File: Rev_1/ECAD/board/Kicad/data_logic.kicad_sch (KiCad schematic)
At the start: 69 parts, among them SW300 SW_Push, SW301 SW_Push, SW302 SW_Push, SW303 SW_Push, U300 AT28C64B-15PU, U301 74HC245, U302 74HC595, U303 74HC245, U304 4076B, U305 4076B, U306 4076B, U307 4076B

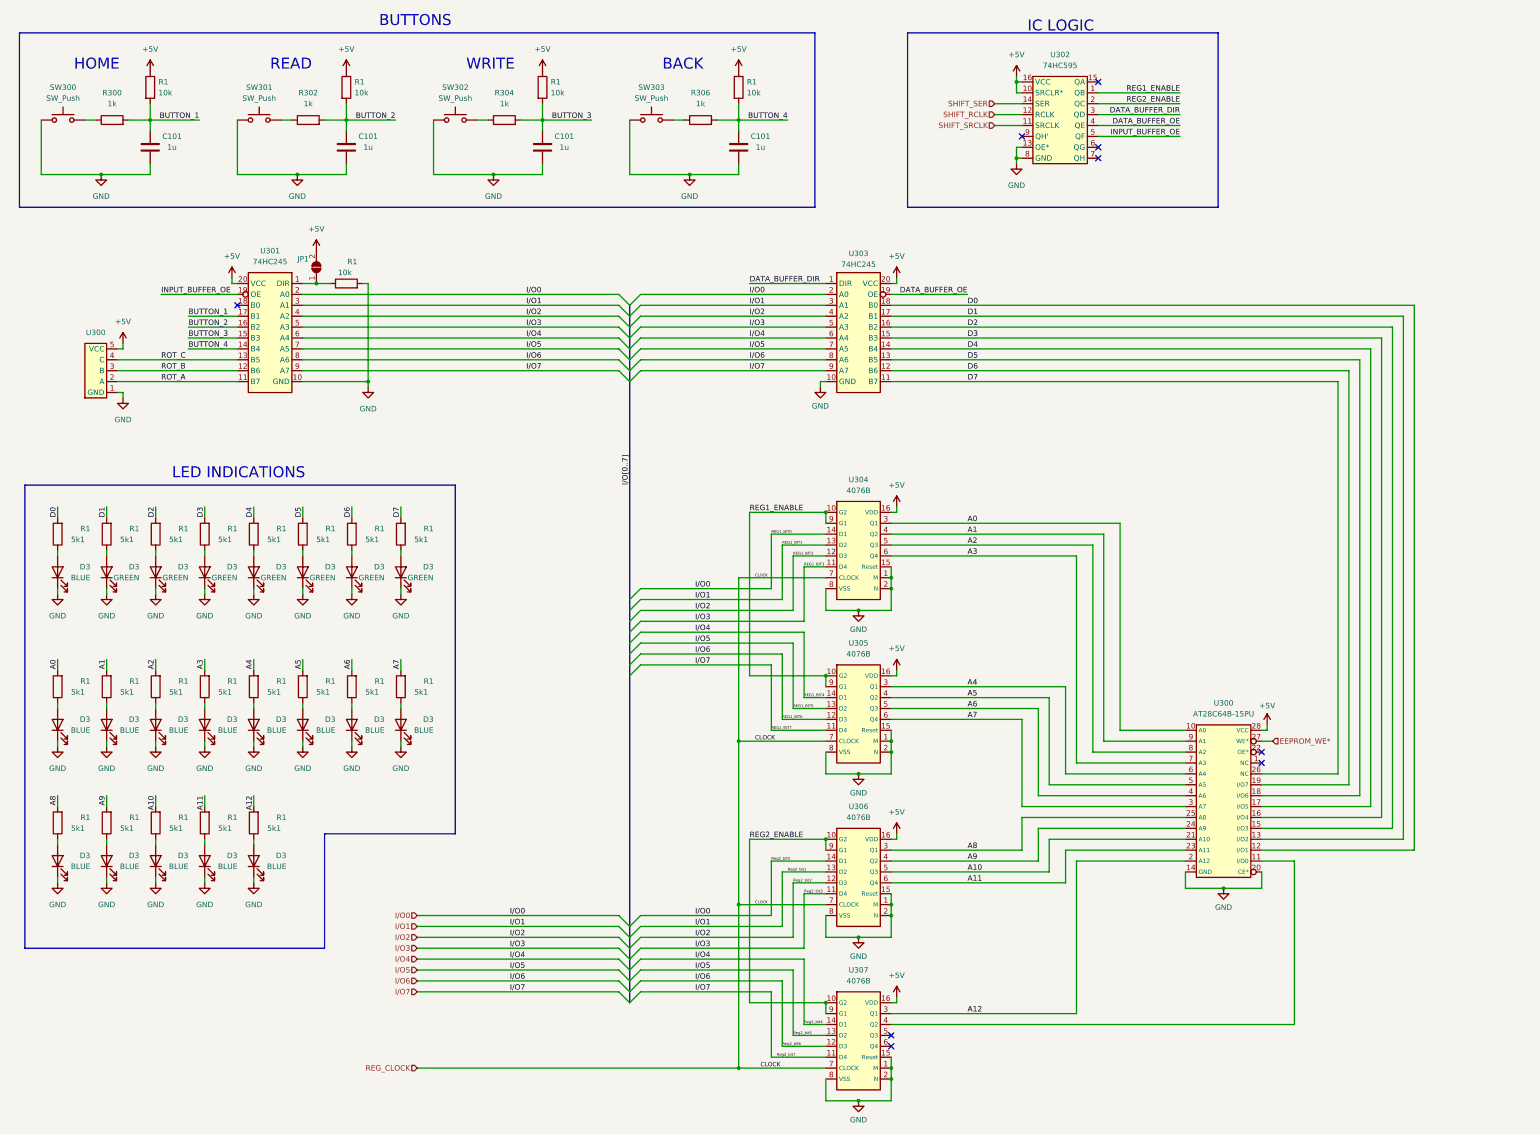
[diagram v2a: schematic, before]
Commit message: Updated Data Logic sheet
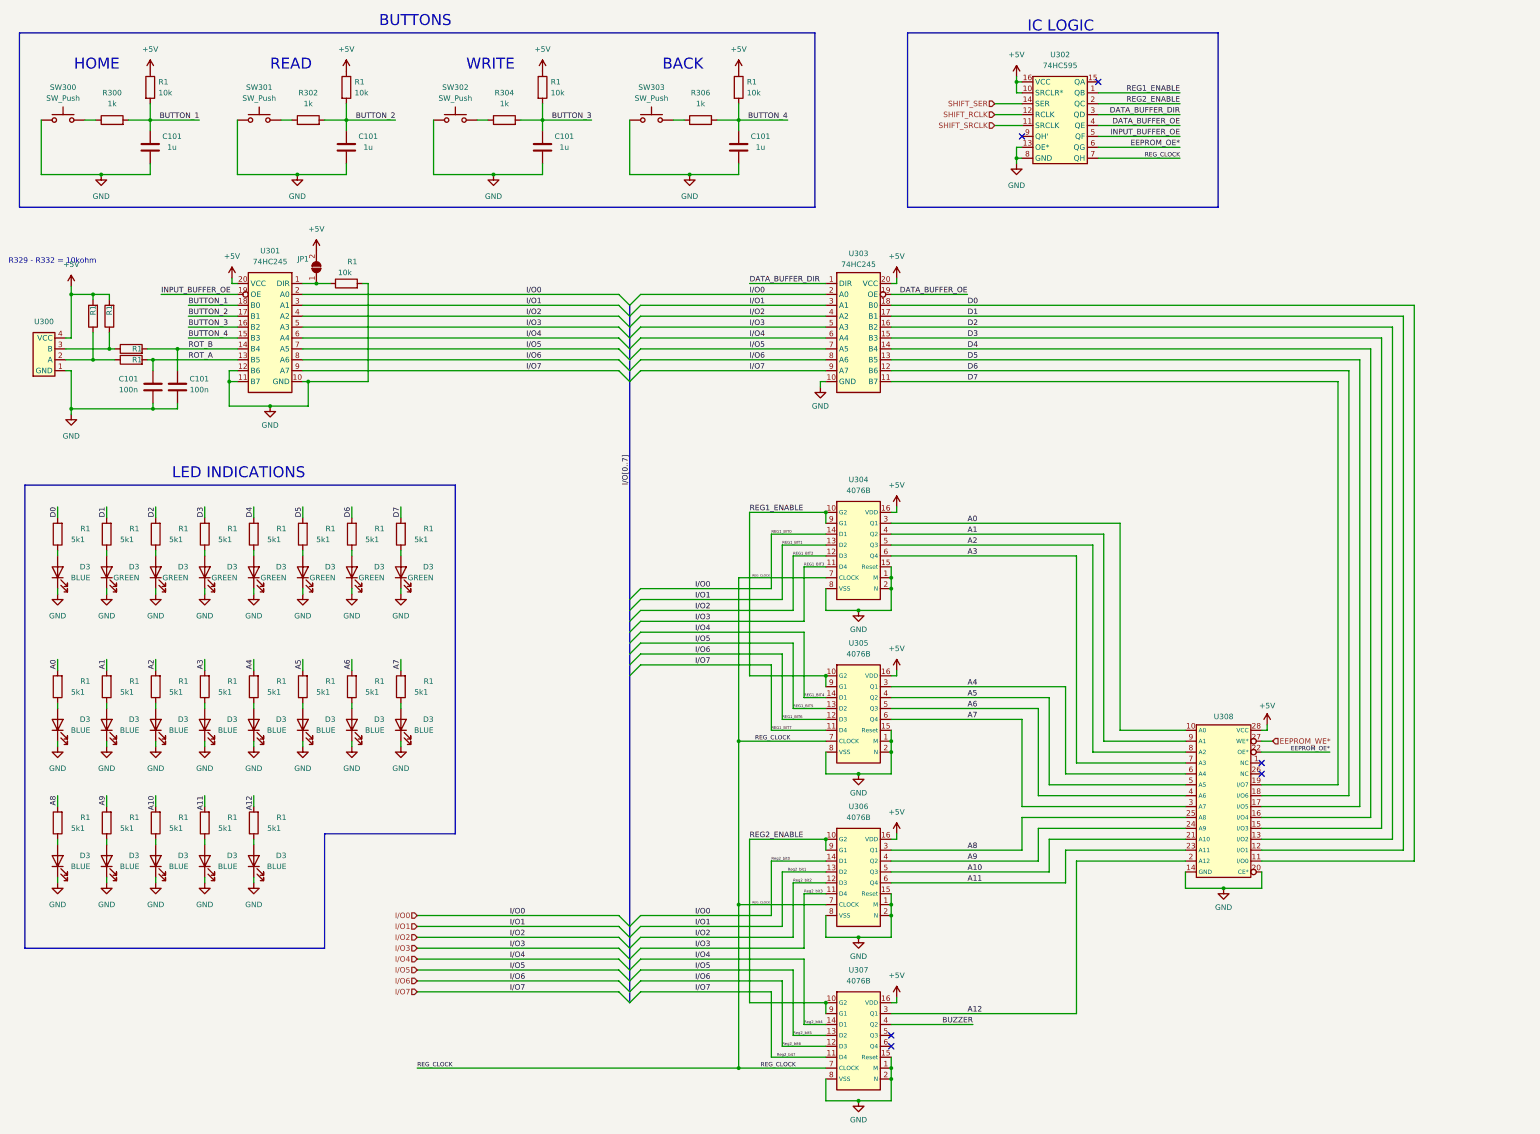
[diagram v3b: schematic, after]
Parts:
- removed U300: ~, symbol EEPROM_PROGRAMER:Rotary_Encoder
- added C101 (x2): 100n, Capacitor_SMD:C_0805_2012Metric_Pad1.18x1.45mm_HandSolder, symbol Device:C
- added R1 (x4): 10k, Resistor_SMD:R_0805_2012Metric_Pad1.20x1.40mm_HandSolder, symbol Device:R
- added U300: ~, symbol EEPROM_PROGRAMMER:Rotary_Encoder
- U308: renamed from U300; value AT28C64B-15PU -> ~; footprint (none) -> EEPROM_PROGRAMMER:AT28C64B-15PU
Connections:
- net ROT_C is gone; now on net ROT_A: U301.13 (B5)
- net +5V: now also R1.2, R1.2, U300.4 (VCC)
- net BUTTON_1: now also U301.18 (B0); no longer U301.17 (B1)
- net BUTTON_2: now also U301.17 (B1); no longer U301.16 (B2)
- net BUTTON_3: now also U301.16 (B2); no longer U301.15 (B3)
- net BUTTON_4: now also U301.15 (B3); no longer U301.14 (B4)
- net D0: now also U308.11 (I/O0); no longer U308.12 (I/O1)
- net D1: now also U308.12 (I/O1); no longer U308.13 (I/O2)
- net D2: now also U308.13 (I/O2); no longer U308.15 (I/O3)
- net D3: now also U308.15 (I/O3); no longer U308.16 (I/O4)
- net D4: now also U308.16 (I/O4); no longer U308.17 (I/O5)
- net D5: now also U308.17 (I/O5); no longer U308.18 (I/O6)
- net D6: now also U308.18 (I/O6); no longer U308.19 (I/O7)
- net D7: now also U308.19 (I/O7); no longer U308.26 (NC)
- net GND: now also U301.11 (B7), U301.12 (B6), C101.1, C101.1, U300.1 (GND)
- net REG_CLOCK: now also U302.7 (QH)
- net ROT_A: now also C101.2, R1.2; no longer U301.11 (B7)
- net ROT_B: now also U301.14 (B4), C101.2, R1.2; no longer U301.12 (B6)
- net BUZZER: now reaches U307.4 (Q2)
- net BUZZER: no longer U308.11 (I/O0)
- net EEPROM_OE*: now reaches U308.22 (OE*)
- net EEPROM_OE*: now also U302.6 (QG)
- new net: R1.1, R1.1, U300.3 (B)
- new net: R1.1, R1.1, U300.2 (A)
- no-connect marks 9 -> 6
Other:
- note added: "R329 - R332 = 10kohm"

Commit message: Changed from 4-bit registers to shift registers
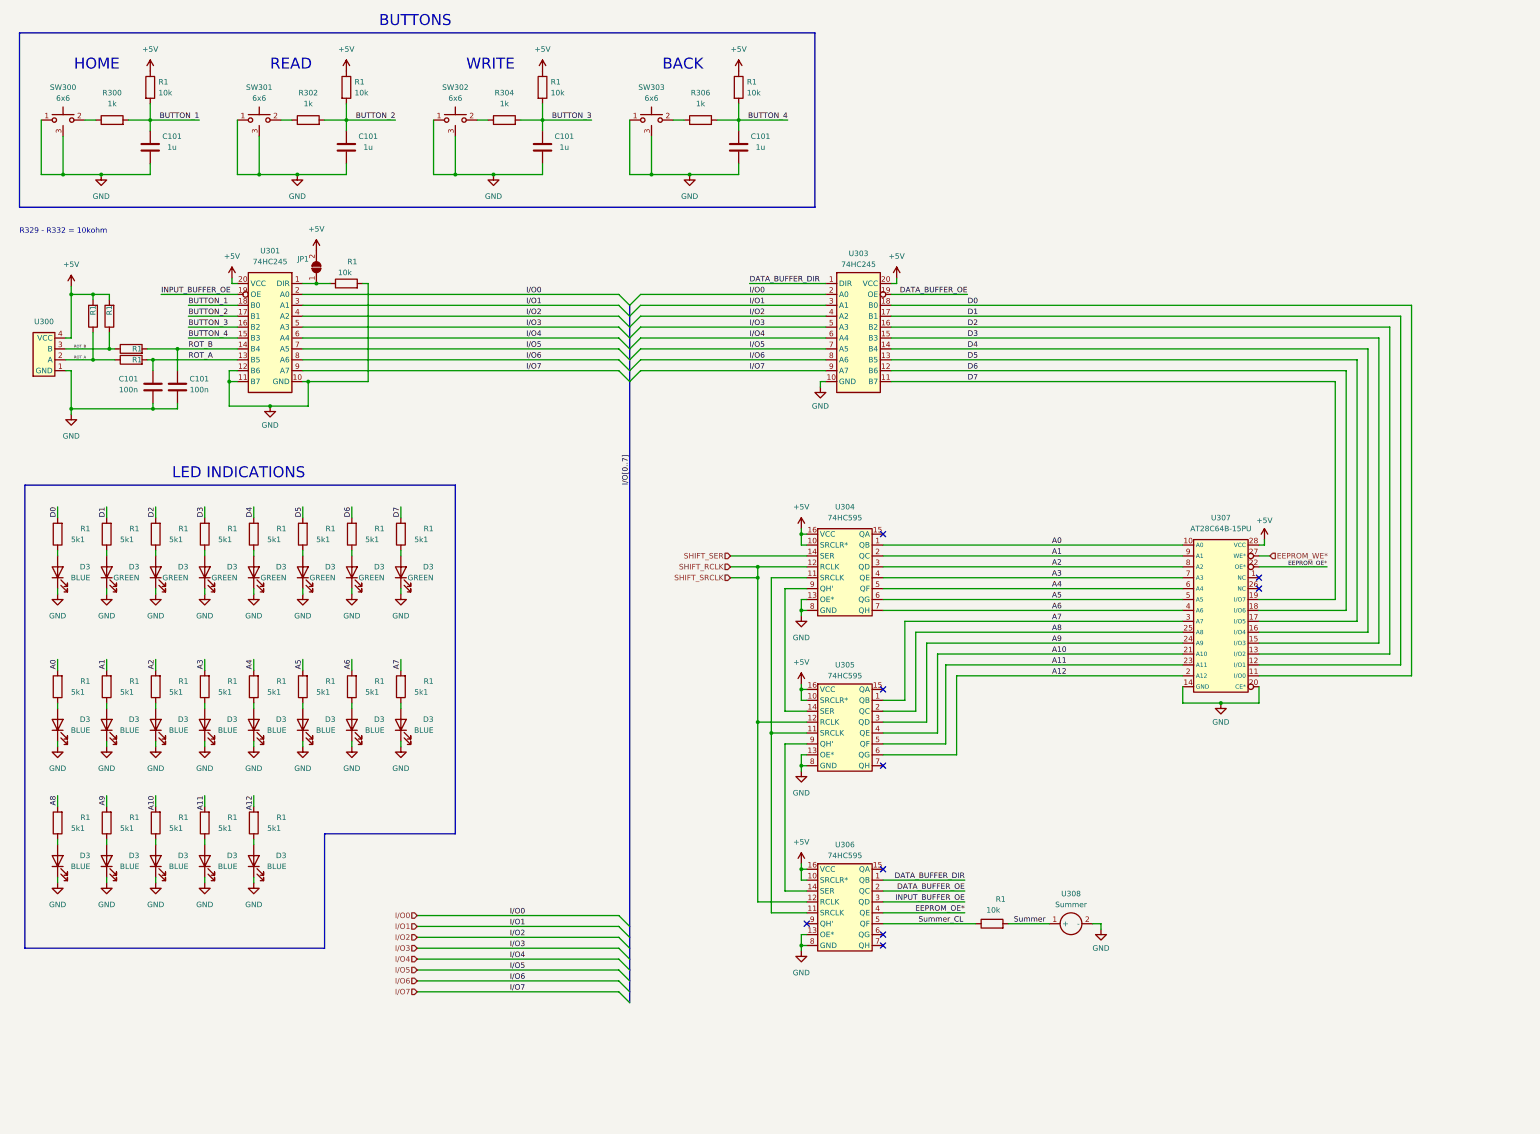
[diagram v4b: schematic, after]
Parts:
- removed SW300, SW301, SW302, SW303: SW_Push, symbol Switch:SW_Push
- removed U302: 74HC595, symbol EEPROM_PROGRAMMER:74HC595
- removed U304, U305, U306, U307: 4076B, symbol EEPROM_PROGRAMMER:4076B
- removed U308: ~, EEPROM_PROGRAMMER:AT28C64B-15PU, symbol EEPROM_PROGRAMMER:AT28C64B-15PU
- added R1: 10k, Resistor_SMD:R_0805_2012Metric_Pad1.20x1.40mm_HandSolder, symbol Device:R
- added SW300, SW301, SW302, SW303: 6x6, EEPROM_PROGRAMMER:SMD_Button, symbol EEPROM_PROGRAMMER:Button
- added U304, U305, U306: 74HC595, EEPROM_PROGRAMMER:74HC595D, symbol EEPROM_PROGRAMMER:74HC595
- added U307: AT28C64B-15PU, EEPROM_PROGRAMMER:AT28C64B-15PU, symbol EEPROM_PROGRAMMER:AT28C64B-15PU
- added U308: Summer, EEPROM_PROGRAMMER:Summer, symbol EEPROM_PROGRAMMER:Summer
- U300: footprint (none) -> EEPROM_PROGRAMMER:Rotary_Encoder
- U301, U303: footprint (none) -> EEPROM_PROGRAMMER:74HC245
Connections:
- net +5V: now also U304.10 (SRCLR*), U304.16 (VCC), U305.10 (SRCLR*), U305.16 (VCC), U306.10 (SRCLR*), U306.16 (VCC), U307.28 (VCC)
- net A0: now also U304.1 (QB), U307.10 (A0)
- net A1: now also U304.2 (QC), U307.9 (A1)
- net A10: now also U305.4 (QE), U307.21 (A10)
- net A11: now also U305.5 (QF), U307.23 (A11)
- net A12: now also U305.6 (QG), U307.2 (A12)
- net A2: now also U304.3 (QD), U307.8 (A2)
- net A3: now also U304.4 (QE), U307.7 (A3)
- net A4: now also U304.5 (QF), U307.6 (A4)
- net A5: now also U304.6 (QG), U307.5 (A5)
- net A6: now also U304.7 (QH), U307.4 (A6)
- net A7: now also U305.1 (QB), U307.3 (A7)
- net A8: now also U305.2 (QC), U307.25 (A8)
- net A9: now also U305.3 (QD), U307.24 (A9)
- net D0: now also U307.11 (I/O0)
- net D1: now also U307.12 (I/O1)
- net D2: now also U307.13 (I/O2)
- net D3: now also U307.15 (I/O3)
- net D4: now also U307.16 (I/O4)
- net D5: now also U307.17 (I/O5)
- net D6: now also U307.18 (I/O6)
- net D7: now also U307.19 (I/O7)
- net DATA_BUFFER_DIR: now also U306.1 (QB)
- net DATA_BUFFER_OE: now also U306.2 (QC)
- net EEPROM_OE*: now also U306.4 (QE), U307.22 (OE*)
- net EEPROM_WE*: now also U307.27 (WE*)
- net GND: now also SW300.1, SW300.3 (GND), SW301.1, SW301.3 (GND), SW302.1, SW302.3 (GND), SW303.1, SW303.3 (GND), U304.13 (OE*), U304.8 (GND), U305.13 (OE*), U305.8 (GND), U306.13 (OE*), U306.8 (GND), U307.14 (GND), U307.20 (CE*), U308.2 (-)
- net INPUT_BUFFER_OE: now also U306.3 (QD)
- net ROT_A: now also R1.1, R1.1, U300.2 (A)
- net ROT_B: now also R1.1, R1.1, U300.3 (B)
- net SHIFT_RCLK: now also U304.12 (RCLK), U305.12 (RCLK), U306.12 (RCLK)
- net SHIFT_SER: now also U304.14 (SER)
- net at R304.1: now also SW302.2
- net at R302.1: now also SW301.2
- net at R300.1: now also SW300.2
- net at R306.1: now also SW303.2
- new net: U304.11 (SRCLK), U305.11 (SRCLK), U306.11 (SRCLK)
- new net: U304.9 (QH'), U305.14 (SER)
- new net: U305.9 (QH'), U306.14 (SER)
- new net Summer: R1.2, U308.1 (+)
- new net Summer_CL: R1.1, U306.5 (QF)
- no-connect marks 6 -> 9
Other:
- note removed: "IC LOGIC"

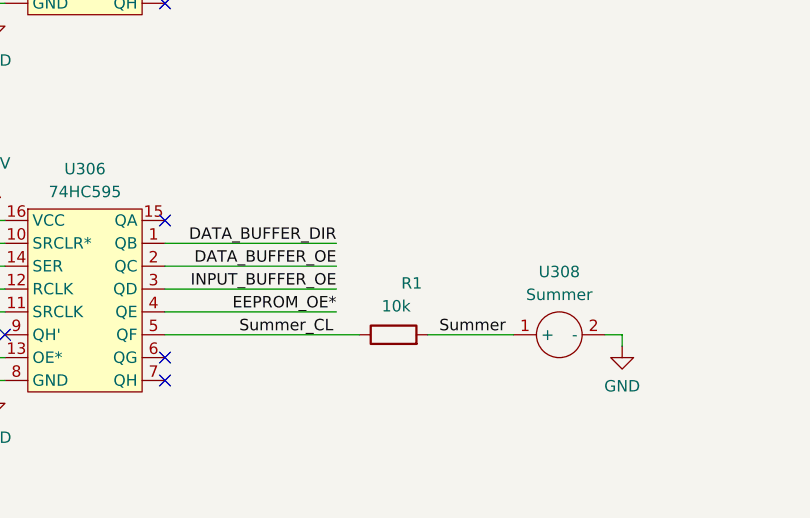
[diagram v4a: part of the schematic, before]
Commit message: Created a pcb file and added labels to footprints
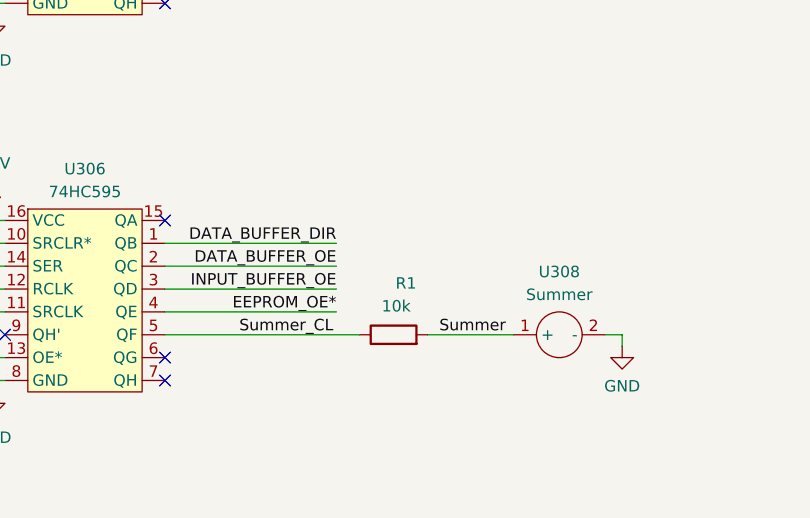
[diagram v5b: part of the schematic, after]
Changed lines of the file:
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@@
   (symbol (lib_id "Device:R") (at 247.015 225.425 90) (unit 1)
     (in_bom yes) (on_board yes) (dnp no)
-    (property "Reference" "R1" (at 250.19 219.71 90)
+    (property "Reference" "R1" (at 249.555 219.71 90)
       (effects (font (size 1.27 1.27)) (justify left))
     )
